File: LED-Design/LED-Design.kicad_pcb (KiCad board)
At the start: 2 copper layers, 162 parts, among them Q1 NMOS, Q2 NMOS, Q3 NMOS, Q4 NMOS, Q5 NMOS, Q6 NMOS, Q7 NMOS, U1 74LS573, U2 74LS573, U3 74LS573, U4 74LS573, U6 74HC164

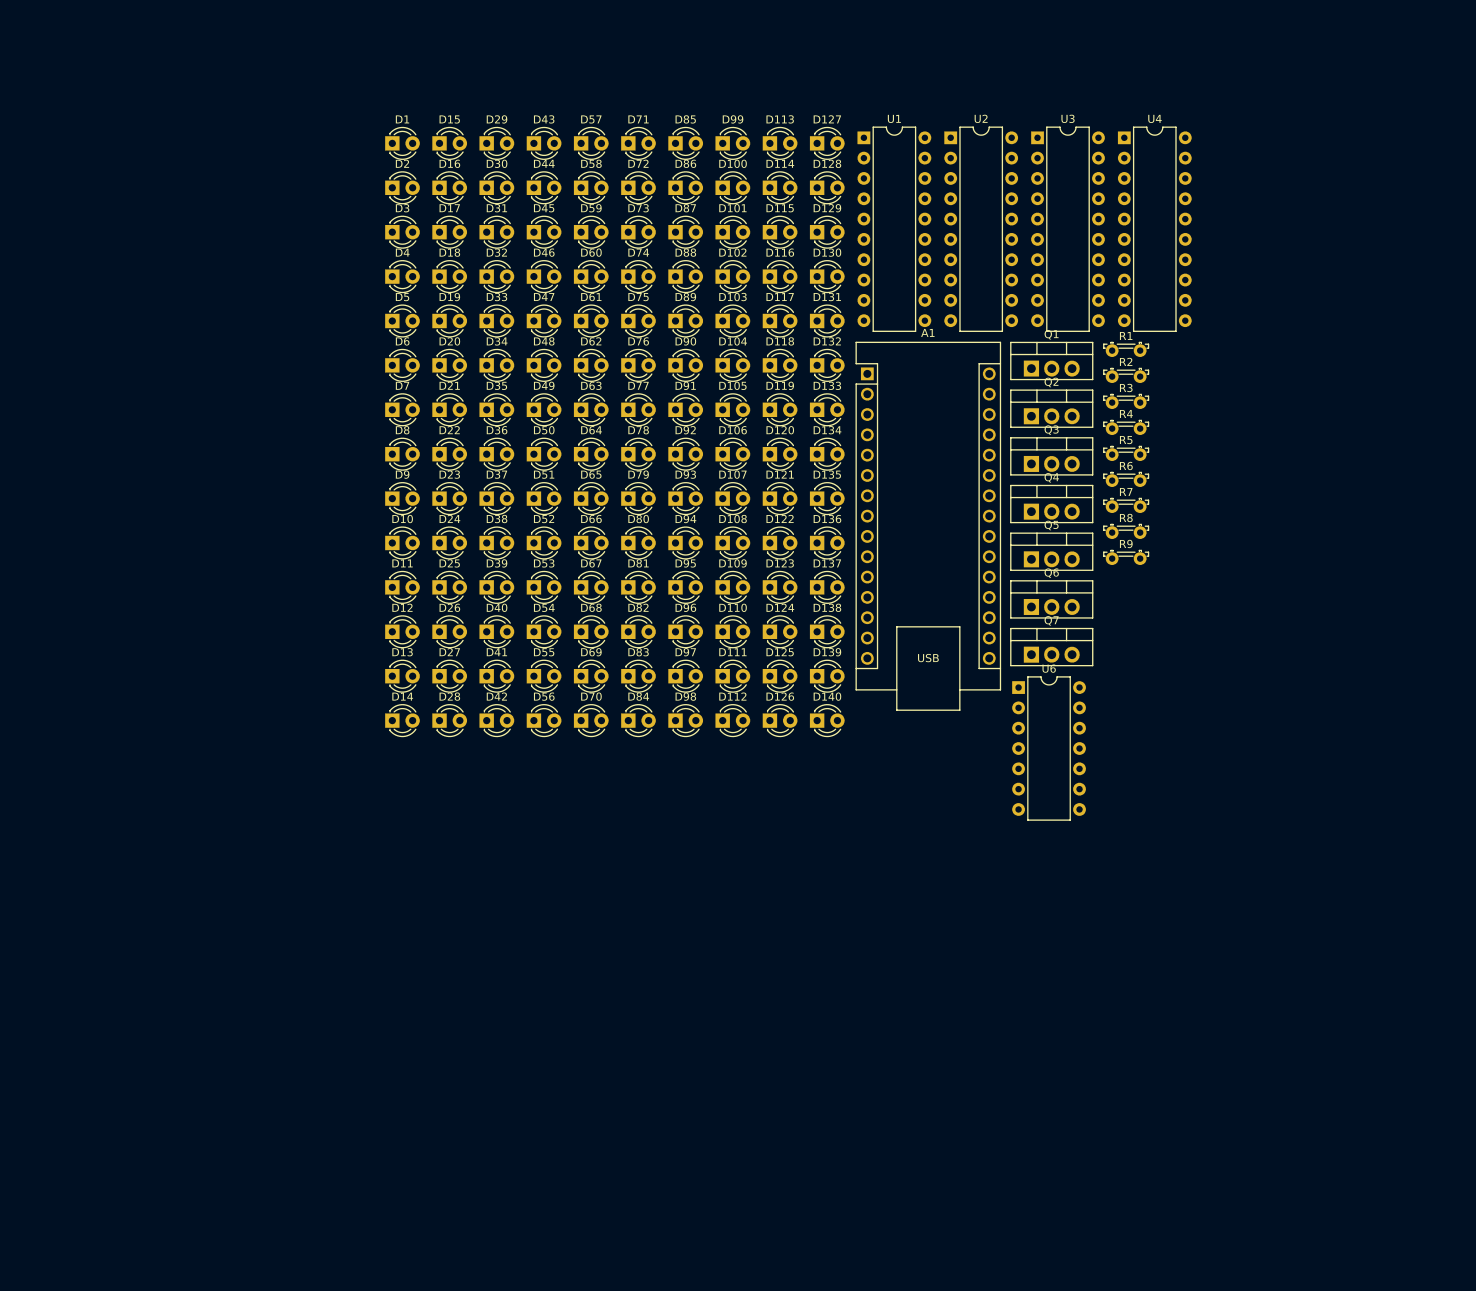
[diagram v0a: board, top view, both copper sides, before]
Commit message: Used the distribute function in PCB Design to correctly align all the LEDs in their matrix. Used an 8mm gap between all LEDs
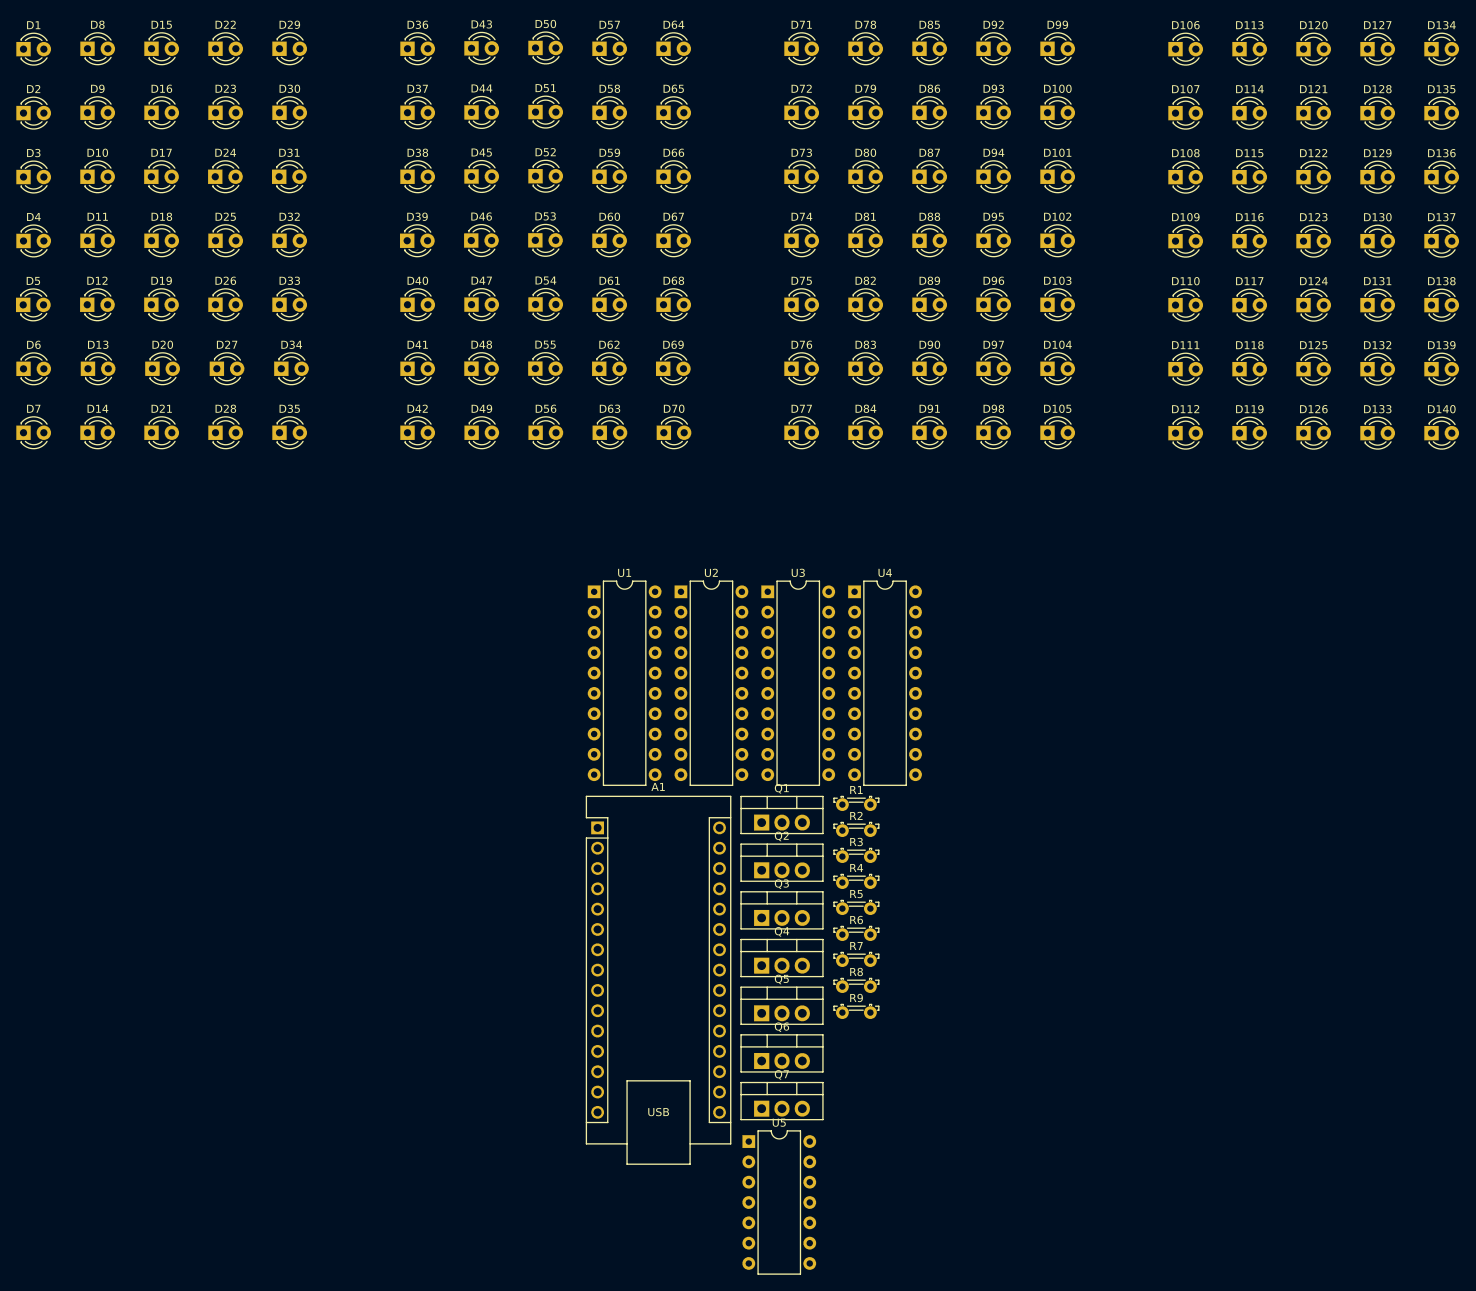
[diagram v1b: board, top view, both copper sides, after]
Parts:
- removed U6: 74HC164, Package_DIP:DIP-14_W7.62mm
- added U5: 74HC164, Package_DIP:DIP-14_W7.62mm, F.Cu at (145.7, 176.6)
- moved D134 92.0 mm to (231.0, 40.0)
- moved D135 90.7 mm to (231.0, 48.0)
- moved D136 89.4 mm to (231.0, 56.0)
- moved D137 88.2 mm to (231.0, 64.0)
- moved D138 87.0 mm to (231.0, 72.0)
- moved D139 85.9 mm to (231.0, 80.0)
- moved D140 84.8 mm to (231.0, 88.0)
- moved D120 83.7 mm to (215.0, 40.0)
- moved D121 82.3 mm to (215.0, 48.0)
- moved D122 80.9 mm to (215.0, 56.0)
- moved D123 79.5 mm to (215.0, 64.0)
- moved D124 78.2 mm to (215.0, 72.0)
- moved D125 77.0 mm to (215.0, 80.0)
- moved D106 75.9 mm to (199.0, 40.0)
- moved D126 75.8 mm to (215.0, 88.0)
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
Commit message: Fixed the assignment of the MOSFET footprints to be GDS.
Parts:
- moved R1 136.8 mm to (25.0, 100.0)
- moved R2 135.6 mm to (25.0, 108.0)
- moved R3 134.7 mm to (25.0, 116.0)
- moved R4 133.9 mm to (25.0, 124.0)
- moved R5 133.3 mm to (25.0, 132.0)
- moved R6 132.8 mm to (25.0, 140.0)
- moved R7 132.5 mm to (25.0, 148.0)
- moved Q1 128.1 mm to (270.0, 100.0)
- moved Q2 127.5 mm to (270.0, 108.0)
- moved Q3 127.0 mm to (270.0, 116.0)
- moved Q4 126.5 mm to (270.0, 124.0)
- moved Q5 126.0 mm to (270.0, 132.0)
- moved Q6 125.6 mm to (270.0, 140.0)
- moved Q7 125.1 mm to (270.0, 148.0)
- moved R9 78.9 mm to (236.0, 154.0)
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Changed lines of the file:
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@@
 	(footprint "OptoDevice:R_LDR_5.2x5.2mm_P3.5mm_Horizontal"
 		(layer "F.Cu")
-		(at 157.36 160.43)
+		(at 236 154)
 		(descr "Resistor, LDR 5.2x5.2, upright, see http://cdn-reichelt.de/documents/datenblatt/A500/M996011A.pdf")
 		(tags "Resistor LDR5.2x5.2 ")
@@
 	(footprint "Package_TO_SOT_THT:TO-220-3_Vertical"
 		(layer "F.Cu")
-		(at 147.27 148.6)
+		(at 270 116)
 		(descr "TO-220-3, Vertical, RM 2.54mm, see https://www.vishay.com/docs/66542/to-220-1.pdf")
 		(tags "TO-220-3 Vertical RM 2.54mm")
@@
 			)
 		)
-		(sheetname "Root")
-		(sheetfile "LED-Design.kicad_sch")
 		(attr through_hole)
 		(fp_line
@@
 			)
 		)
-		(pad "1" thru_hole rect
-			(at 0 0)
-			(size 1.905 2)
+		(pad "1" thru_hole circle
+			(at 2.54 0)
+			(size 1.905 1.905)
 			(drill 1.1)
 			(layers "*.Cu" "*.Mask")
@@
 			(pintype "passive")
 		)
-		(pad "2" thru_hole oval
-			(at 2.54 0)
+		(pad "2" thru_hole rect
+			(at 0 0)
 			(size 1.905 2)
 			(drill 1.1)
@@
 	(footprint "OptoDevice:R_LDR_5.2x5.2mm_P3.5mm_Horizontal"
 		(layer "F.Cu")
-		(at 157.36 144.18)
+		(at 25 124)
 		(descr "Resistor, LDR 5.2x5.2, upright, see http://cdn-reichelt.de/documents/datenblatt/A500/M996011A.pdf")
 		(tags "Resistor LDR5.2x5.2 ")
@@
 	(footprint "Package_TO_SOT_THT:TO-220-3_Vertical"
 		(layer "F.Cu")
-		(at 147.27 160.52)
+		(at 270 132)
 		(descr "TO-220-3, Vertical, RM 2.54mm, see https://www.vishay.com/docs/66542/to-220-1.pdf")
 		(tags "TO-220-3 Vertical RM 2.54mm")
@@
 			)
 		)
-		(sheetname "Root")
-		(sheetfile "LED-Design.kicad_sch")
 		(attr through_hole)
 		(fp_line
@@
 			)
 		)
-		(pad "1" thru_hole rect
-			(at 0 0)
-			(size 1.905 2)
+		(pad "1" thru_hole circle
+			(at 2.54 0)
+			(size 1.905 1.905)
 			(drill 1.1)
 			(layers "*.Cu" "*.Mask")
@@
 			(pintype "passive")
 		)
-		(pad "2" thru_hole oval
-			(at 2.54 0)
+		(pad "2" thru_hole rect
+			(at 0 0)
 			(size 1.905 2)
 			(drill 1.1)
@@
 	(footprint "Package_TO_SOT_THT:TO-220-3_Vertical"
 		(layer "F.Cu")
-		(at 147.27 154.56)
+		(at 270 124)
 		(descr "TO-220-3, Vertical, RM 2.54mm, see https://www.vishay.com/docs/66542/to-220-1.pdf")
 		(tags "TO-220-3 Vertical RM 2.54mm")
@@
 			)
 		)
-		(sheetname "Root")
-		(sheetfile "LED-Design.kicad_sch")
 		(attr through_hole)
 		(fp_line
@@
 			)
 		)
-		(pad "1" thru_hole rect
-			(at 0 0)
-			(size 1.905 2)
+		(pad "1" thru_hole circle
+			(at 2.54 0)
+			(size 1.905 1.905)
 			(drill 1.1)
 			(layers "*.Cu" "*.Mask")
@@
 			(pintype "passive")
 		)
-		(pad "2" thru_hole oval
-			(at 2.54 0)
+		(pad "2" thru_hole rect
+			(at 0 0)
 			(size 1.905 2)
 			(drill 1.1)
@@
 	(footprint "OptoDevice:R_LDR_5.2x5.2mm_P3.5mm_Horizontal"
 		(layer "F.Cu")
-		(at 157.36 134.43)
+		(at 25 100)
 		(descr "Resistor, LDR 5.2x5.2, upright, see http://cdn-reichelt.de/documents/datenblatt/A500/M996011A.pdf")
 		(tags "Resistor LDR5.2x5.2 ")
@@
 	(footprint "OptoDevice:R_LDR_5.2x5.2mm_P3.5mm_Horizontal"
 		(layer "F.Cu")
-		(at 157.36 137.68)
+		(at 25 108)
 		(descr "Resistor, LDR 5.2x5.2, upright, see http://cdn-reichelt.de/documents/datenblatt/A500/M996011A.pdf")
 		(tags "Resistor LDR5.2x5.2 ")
@@
 	(footprint "OptoDevice:R_LDR_5.2x5.2mm_P3.5mm_Horizontal"
 		(layer "F.Cu")
-		(at 157.36 140.93)
+		(at 25 116)
 		(descr "Resistor, LDR 5.2x5.2, upright, see http://cdn-reichelt.de/documents/datenblatt/A500/M996011A.pdf")
 		(tags "Resistor LDR5.2x5.2 ")
@@
 	(footprint "Package_TO_SOT_THT:TO-220-3_Vertical"
 		(layer "F.Cu")
-		(at 147.27 136.68)
+		(at 270 100)
 		(descr "TO-220-3, Vertical, RM 2.54mm, see https://www.vishay.com/docs/66542/to-220-1.pdf")
 		(tags "TO-220-3 Vertical RM 2.54mm")
@@
 			)
 		)
-		(sheetname "Root")
-		(sheetfile "LED-Design.kicad_sch")
 		(attr through_hole)
 		(fp_line
@@
 			)
 		)
-		(pad "1" thru_hole rect
-			(at 0 0)
-			(size 1.905 2)
+		(pad "1" thru_hole circle
+			(at 2.54 0)
+			(size 1.905 1.905)
 			(drill 1.1)
 			(layers "*.Cu" "*.Mask")
@@
 			(pintype "passive")
 		)
-		(pad "2" thru_hole oval
-			(at 2.54 0)
-			(size 1.905 2)
+		(pad "2" thru_hole rect
+			(at 0 0)
+			(size 1.905 1.905)
 			(drill 1.1)
 			(layers "*.Cu" "*.Mask")
@@
 	(footprint "OptoDevice:R_LDR_5.2x5.2mm_P3.5mm_Horizontal"
 		(layer "F.Cu")
-		(at 157.36 157.18)
+		(at 223.5 158.5)
 		(descr "Resistor, LDR 5.2x5.2, upright, see http://cdn-reichelt.de/documents/datenblatt/A500/M996011A.pdf")
 		(tags "Resistor LDR5.2x5.2 ")
@@
 	(footprint "OptoDevice:R_LDR_5.2x5.2mm_P3.5mm_Horizontal"
 		(layer "F.Cu")
-		(at 157.36 150.68)
+		(at 25 140)
 		(descr "Resistor, LDR 5.2x5.2, upright, see http://cdn-reichelt.de/documents/datenblatt/A500/M996011A.pdf")
 		(tags "Resistor LDR5.2x5.2 ")
@@
 	(footprint "Package_TO_SOT_THT:TO-220-3_Vertical"
 		(layer "F.Cu")
-		(at 147.27 166.48)
+		(at 270 140)
 		(descr "TO-220-3, Vertical, RM 2.54mm, see https://www.vishay.com/docs/66542/to-220-1.pdf")
 		(tags "TO-220-3 Vertical RM 2.54mm")
@@
 			)
 		)
-		(sheetname "Root")
-		(sheetfile "LED-Design.kicad_sch")
 		(attr through_hole)
 		(fp_line
@@
 			)
 		)
-		(pad "1" thru_hole rect
-			(at 0 0)
-			(size 1.905 2)
+		(pad "1" thru_hole circle
+			(at 2.54 0)
+			(size 1.905 1.905)
 			(drill 1.1)
 			(layers "*.Cu" "*.Mask")
@@
 			(pintype "passive")
 		)
-		(pad "2" thru_hole oval
-			(at 2.54 0)
+		(pad "2" thru_hole rect
+			(at 0 0)
 			(size 1.905 2)
 			(drill 1.1)
@@
 	(footprint "OptoDevice:R_LDR_5.2x5.2mm_P3.5mm_Horizontal"
 		(layer "F.Cu")
-		(at 157.36 147.43)
+		(at 25 132)
 		(descr "Resistor, LDR 5.2x5.2, upright, see http://cdn-reichelt.de/documents/datenblatt/A500/M996011A.pdf")
 		(tags "Resistor LDR5.2x5.2 ")
@@
 	(footprint "Package_TO_SOT_THT:TO-220-3_Vertical"
 		(layer "F.Cu")
-		(at 147.27 172.44)
+		(at 270 148)
 		(descr "TO-220-3, Vertical, RM 2.54mm, see https://www.vishay.com/docs/66542/to-220-1.pdf")
 		(tags "TO-220-3 Vertical RM 2.54mm")
@@
 			)
 		)
-		(sheetname "Root")
-		(sheetfile "LED-Design.kicad_sch")
 		(attr through_hole)
 		(fp_line
@@
 			)
 		)
-		(pad "1" thru_hole rect
-			(at 0 0)
-			(size 1.905 2)
+		(pad "1" thru_hole circle
+			(at 2.54 0)
+			(size 1.905 1.905)
 			(drill 1.1)
 			(layers "*.Cu" "*.Mask")
@@
 			(pintype "passive")
 		)
-		(pad "2" thru_hole oval
-			(at 2.54 0)
+		(pad "2" thru_hole rect
+			(at 0 0)
 			(size 1.905 2)
 			(drill 1.1)
@@
 	(footprint "Package_TO_SOT_THT:TO-220-3_Vertical"
 		(layer "F.Cu")
-		(at 147.27 142.64)
+		(at 270 108)
 		(descr "TO-220-3, Vertical, RM 2.54mm, see https://www.vishay.com/docs/66542/to-220-1.pdf")
 		(tags "TO-220-3 Vertical RM 2.54mm")
@@
 			)
 		)
-		(sheetname "Root")
-		(sheetfile "LED-Design.kicad_sch")
 		(attr through_hole)
 		(fp_line
@@
 			)
 		)
-		(pad "1" thru_hole rect
-			(at 0 0)
-			(size 1.905 2)
+		(pad "1" thru_hole circle
+			(at 2.54 0)
+			(size 1.905 1.905)
 			(drill 1.1)
 			(layers "*.Cu" "*.Mask")
@@
 			(pintype "passive")
 		)
-		(pad "2" thru_hole oval
-			(at 2.54 0)
-			(size 1.905 2)
+		(pad "2" thru_hole rect
+			(at 0 0)
+			(size 1.905 1.905)
 			(drill 1.1)
 			(layers "*.Cu" "*.Mask")
@@
 	(footprint "OptoDevice:R_LDR_5.2x5.2mm_P3.5mm_Horizontal"
 		(layer "F.Cu")
-		(at 157.36 153.93)
+		(at 25 148)
 		(descr "Resistor, LDR 5.2x5.2, upright, see http://cdn-reichelt.de/documents/datenblatt/A500/M996011A.pdf")
 		(tags "Resistor LDR5.2x5.2 ")

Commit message: Added footprints for ground and power
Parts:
- added GND1: ~, TerminalBlock_MetzConnect:TerminalBlock_MetzConnect_360271_1x01_Horizontal_ScrewM3.0_Boxed, F.Cu at (59.5, 146.5)
- added PWR1: 24V, 0.160A, TerminalBlock_MetzConnect:TerminalBlock_MetzConnect_360271_1x01_Horizontal_ScrewM3.0_Boxed, F.Cu at (73.5, 146.5)
- moved R8 128.6 mm to (95.5, 146.5)
- moved U5 108.0 mm to (240.0, 124.0)
- moved R9 84.8 mm to (151.5, 146.5)
- moved U1 65.5 mm to (61.1, 113.8), turned to 90 degrees
- moved U4 46.1 mm to (204.6, 113.9), turned to 90 degrees
- moved A1 34.0 mm to (158.1, 124.0), turned to -90 degrees
- moved U2 28.9 mm to (108.9, 113.9), turned to 90 degrees
- moved U3 10.6 mm to (156.7, 113.9), turned to 90 degrees
- moved Q7 1.50 mm to (270.0, 146.5)
- moved R7 1.50 mm to (25.0, 146.5)
- moved Q6 1.25 mm to (270.0, 138.8)
- moved R6 1.25 mm to (25.0, 138.8)
- moved Q5 1.00 mm to (270.0, 131.0)
- moved R5 1.00 mm to (25.0, 131.0)
- moved Q4 0.75 mm to (270.0, 123.2)
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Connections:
- net +24V renamed Net-(PWR1-Pin_1)
- net GND renamed Net-(GND1-Pin_1)
- Q1 pad 1: Net-(D1-A) -> Net-(Q1-G)
- Q1 pad 2: Net-(Q1-G) -> Net-(D1-A)
- Q2 pad 1: Net-(D100-A) -> Net-(Q2-G)
- Q2 pad 2: Net-(Q2-G) -> Net-(D100-A)
- Q3 pad 1: Net-(D10-A) -> Net-(Q3-G)
- Q3 pad 2: Net-(Q3-G) -> Net-(D10-A)
- Q4 pad 1: Net-(D102-A) -> Net-(Q4-G)
- Q4 pad 2: Net-(Q4-G) -> Net-(D102-A)
- Q5 pad 1: Net-(D103-A) -> Net-(Q5-G)
- Q5 pad 2: Net-(Q5-G) -> Net-(D103-A)
- Q6 pad 1: Net-(D104-A) -> Net-(Q6-G)
- Q6 pad 2: Net-(Q6-G) -> Net-(D104-A)
- Q7 pad 1: Net-(D105-A) -> Net-(Q7-G)
- Q7 pad 2: Net-(Q7-G) -> Net-(D105-A)

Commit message: Added the majority of traces
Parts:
- moved GND1 219.8 mm to (274.0, 98.5)
- moved R8 72.6 mm to (25.0, 164.0)
- moved PWR1 68.2 mm to (25.0, 98.5)
- moved R9 22.7 mm to (166.0, 164.0)
- moved Q1 10.0 mm to (269.0, 110.0)
- moved Q2 10.0 mm to (269.0, 117.8)
- moved Q3 10.0 mm to (269.0, 125.5)
- moved Q4 10.0 mm to (269.0, 133.2)
- moved Q5 10.0 mm to (269.0, 141.0)
- moved Q6 10.0 mm to (269.0, 148.8)
- moved Q7 10.0 mm to (269.0, 156.5)
- moved R1 9.50 mm to (25.0, 109.5)
- moved R2 9.50 mm to (25.0, 117.2)
- moved R3 9.50 mm to (25.0, 125.0)
- moved R4 9.50 mm to (25.0, 132.8)
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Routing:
- net Net-(D1-A): track 0.00 -> 464.5 mm
- net Net-(D10-A): track 0.00 -> 461.8 mm
- net Net-(D100-A): track 0.00 -> 461.2 mm
- net Net-(D102-A): track 0.00 -> 457.0 mm
- net Net-(D103-A): track 0.00 -> 454.3 mm
- net Net-(D104-A): track 0.00 -> 451.8 mm
- net Net-(D105-A): track 0.00 -> 448.7 mm
- net Net-(GND1-Pin_1): track 0.00 -> 227.2 mm
- net Net-(A1-VIN): track 0.00 -> 162.3 mm
- net Net-(D134-K): track 0.00 -> 70.9 mm
- net Net-(D100-K): track 0.00 -> 70.9 mm
- net Net-(D36-K): track 0.00 -> 70.9 mm
- net Net-(D64-K): track 0.00 -> 70.8 mm
- net Net-(D1-K): track 0.00 -> 70.8 mm
- net Net-(D71-K): track 0.00 -> 70.8 mm
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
